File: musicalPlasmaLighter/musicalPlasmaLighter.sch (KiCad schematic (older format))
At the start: 13 parts, among them U1 ATtiny85-20SU, U2 LTC4054ES5-4.2, U3 74HCT00

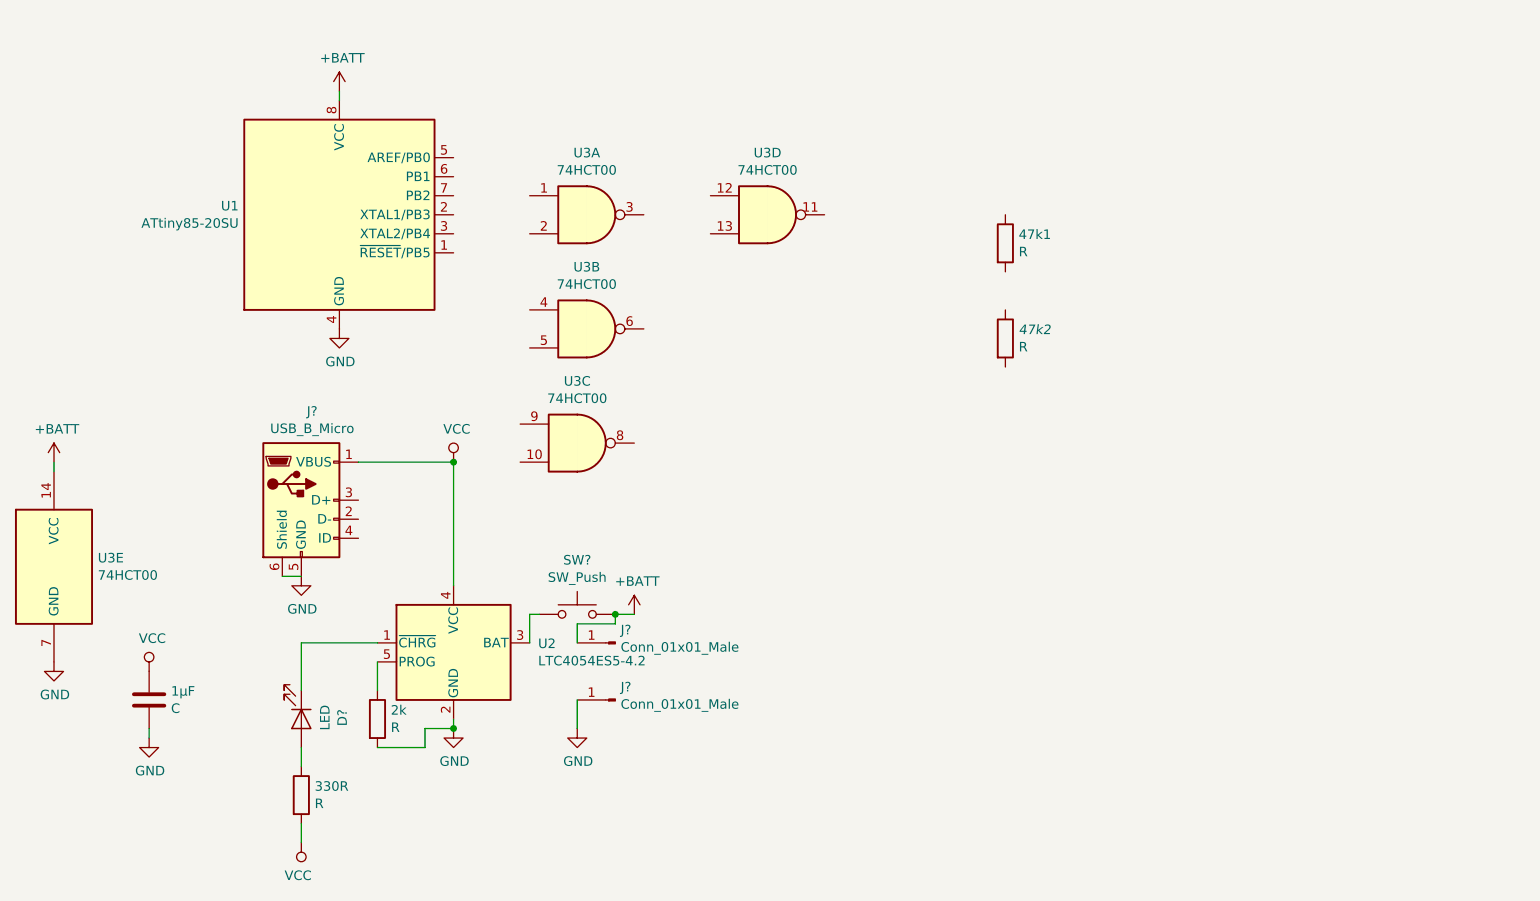
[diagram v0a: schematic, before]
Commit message: updated schematics
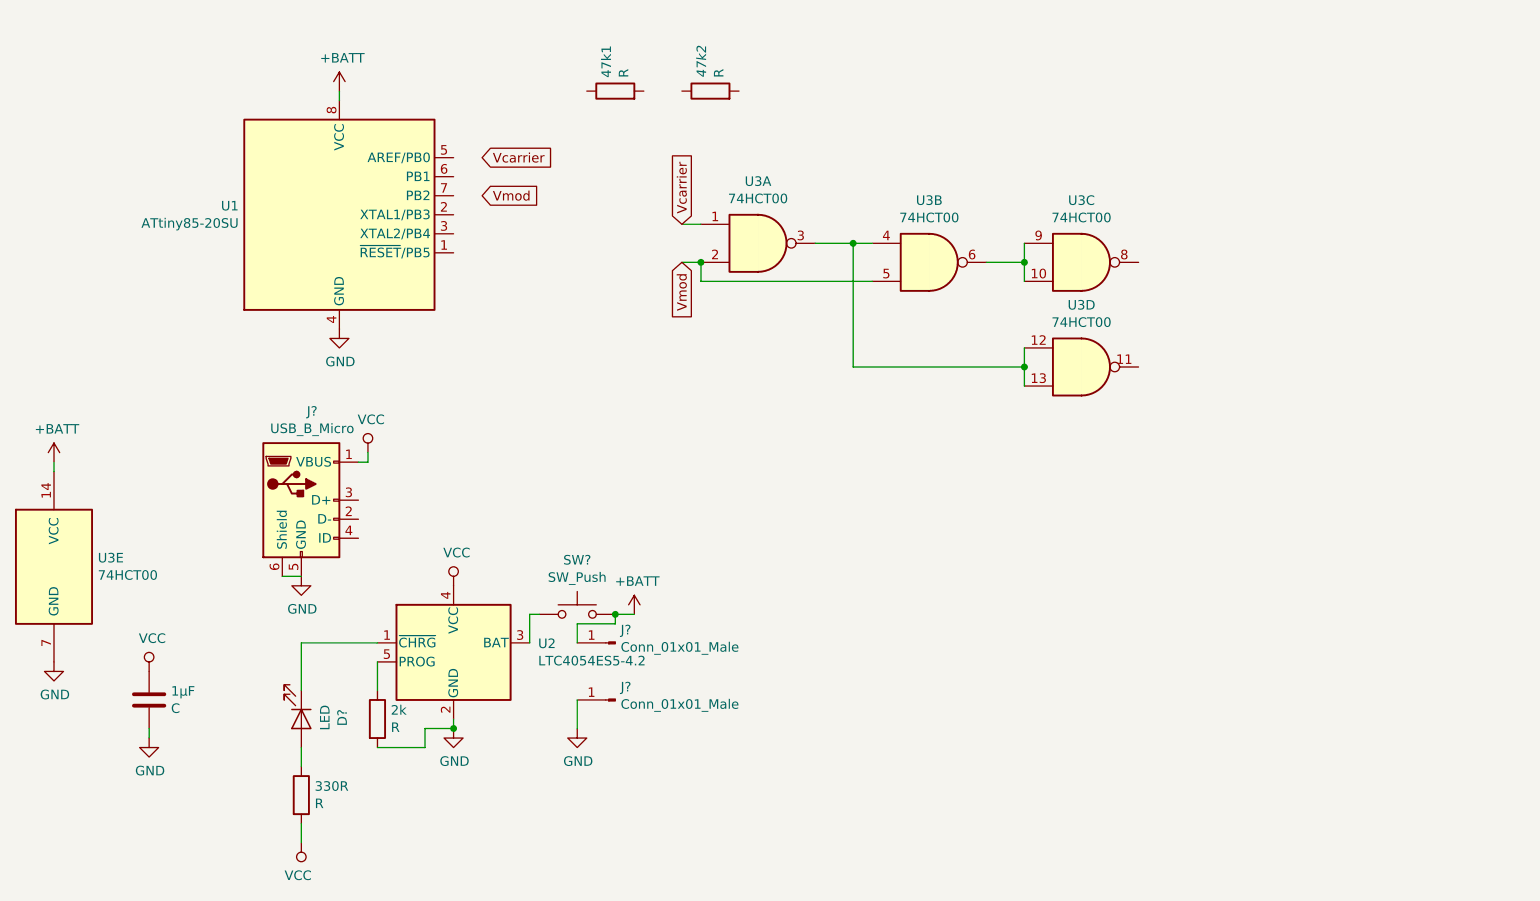
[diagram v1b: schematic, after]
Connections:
- net Vcarrier: now reaches U3.1
- net Vmod: now reaches U3.2
- net Vmod: now also U3.5
- net at U3.3: now also U3.12, U3.13, U3.4
- net at U3.6: now also U3.10, U3.9
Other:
- moved on the sheet: 47k1, 47k2, U3A, U3B, U3C, U3D
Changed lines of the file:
@@
 L 74xx:74HCT00 U3
 U 1 1 5D7430DD
-P 4000 1750
-F 0 "U3" H 4000 2075 50  0000 C CNN
-F 1 "74HCT00" H 4000 1984 50  0000 C CNN
-F 2 "Package_SO:TSSOP-14_4.4x5mm_P0.65mm" H 4000 1750 50  0001 C CNN
-F 3 "http://www.ti.com/lit/gpn/sn74hct00" H 4000 1750 50  0001 C CNN
-	1    4000 1750
+P 4900 1900
+F 0 "U3" H 4900 2225 50  0000 C CNN
+F 1 "74HCT00" H 4900 2134 50  0000 C CNN
+F 2 "Package_SO:TSSOP-14_4.4x5mm_P0.65mm" H 4900 1900 50  0001 C CNN
+F 3 "http://www.ti.com/lit/gpn/sn74hct00" H 4900 1900 50  0001 C CNN
+	1    4900 1900
 	1    0    0    -1
 $EndComp
@@
 L 74xx:74HCT00 U3
 U 2 1 5D744372
-P 4000 2350
-F 0 "U3" H 4000 2675 50  0000 C CNN
-F 1 "74HCT00" H 4000 2584 50  0000 C CNN
-F 2 "Package_SO:TSSOP-14_4.4x5mm_P0.65mm" H 4000 2350 50  0001 C CNN
-F 3 "http://www.ti.com/lit/gpn/sn74hct00" H 4000 2350 50  0001 C CNN
-	2    4000 2350
+P 5800 2000
+F 0 "U3" H 5800 2325 50  0000 C CNN
+F 1 "74HCT00" H 5800 2234 50  0000 C CNN
+F 2 "Package_SO:TSSOP-14_4.4x5mm_P0.65mm" H 5800 2000 50  0001 C CNN
+F 3 "http://www.ti.com/lit/gpn/sn74hct00" H 5800 2000 50  0001 C CNN
+	2    5800 2000
 	1    0    0    -1
 $EndComp
@@
 L 74xx:74HCT00 U3
 U 3 1 5D745C50
-P 3950 2950
-F 0 "U3" H 3950 3275 50  0000 C CNN
-F 1 "74HCT00" H 3950 3184 50  0000 C CNN
-F 2 "Package_SO:TSSOP-14_4.4x5mm_P0.65mm" H 3950 2950 50  0001 C CNN
-F 3 "http://www.ti.com/lit/gpn/sn74hct00" H 3950 2950 50  0001 C CNN
-	3    3950 2950
+P 6600 2000
+F 0 "U3" H 6600 2325 50  0000 C CNN
+F 1 "74HCT00" H 6600 2234 50  0000 C CNN
+F 2 "Package_SO:TSSOP-14_4.4x5mm_P0.65mm" H 6600 2000 50  0001 C CNN
+F 3 "http://www.ti.com/lit/gpn/sn74hct00" H 6600 2000 50  0001 C CNN
+	3    6600 2000
 	1    0    0    -1
 $EndComp
@@
 L 74xx:74HCT00 U3
 U 4 1 5D74715B
-P 4950 1750
-F 0 "U3" H 4950 2075 50  0000 C CNN
-F 1 "74HCT00" H 4950 1984 50  0000 C CNN
-F 2 "Package_SO:TSSOP-14_4.4x5mm_P0.65mm" H 4950 1750 50  0001 C CNN
-F 3 "http://www.ti.com/lit/gpn/sn74hct00" H 4950 1750 50  0001 C CNN
-	4    4950 1750
+P 6600 2550
+F 0 "U3" H 6600 2875 50  0000 C CNN
+F 1 "74HCT00" H 6600 2784 50  0000 C CNN
+F 2 "Package_SO:TSSOP-14_4.4x5mm_P0.65mm" H 6600 2550 50  0001 C CNN
+F 3 "http://www.ti.com/lit/gpn/sn74hct00" H 6600 2550 50  0001 C CNN
+	4    6600 2550
 	1    0    0    -1
 $EndComp
@@
 L Device:R 47k1
 U 1 1 5D750EC0
-P 6200 1900
-F 0 "47k1" H 6270 1946 50  0000 L CNN
-F 1 "R" H 6270 1855 50  0000 L CNN
-F 2 "Resistor_SMD:R_0603_1608Metric" V 6130 1900 50  0001 C CNN
-F 3 "~" H 6200 1900 50  0001 C CNN
-	1    6200 1900
-	1    0    0    -1
+P 4150 1100
+F 0 "47k1" H 4220 1146 50  0000 L CNN
+F 1 "R" H 4220 1055 50  0000 L CNN
+F 2 "Resistor_SMD:R_0603_1608Metric" V 4080 1100 50  0001 C CNN
+F 3 "~" H 4150 1100 50  0001 C CNN
+	1    4150 1100
+	0    -1   -1   0
 $EndComp
 $Comp
 L Device:R 47k2
 U 1 1 5D754E95
-P 6200 2400
-F 0 "47k2" H 6270 2446 50  0000 L CIN
-F 1 "R" H 6270 2355 50  0000 L CNN
-F 2 "Resistor_SMD:R_0603_1608Metric" V 6130 2400 50  0001 C CNN
-F 3 "~" H 6200 2400 50  0001 C CNN
-	1    6200 2400
-	1    0    0    -1
+P 4650 1100
+F 0 "47k2" H 4720 1146 50  0000 L CIN
+F 1 "R" H 4720 1055 50  0000 L CNN
+F 2 "Resistor_SMD:R_0603_1608Metric" V 4580 1100 50  0001 C CNN
+F 3 "~" H 4650 1100 50  0001 C CNN
+	1    4650 1100
+	0    -1   -1   0
 $EndComp
 $Comp
@@
 Wire Wire Line
 	2400 3650 2500 3650
-Wire Wire Line
-	2800 3050 3300 3050
 $Comp
 L power:VCC #PWR?
 U 1 1 5D840F00
-P 3300 3050
-F 0 "#PWR?" H 3300 2900 50  0001 C CNN
-F 1 "VCC" H 3317 3223 50  0000 C CNN
-F 2 "" H 3300 3050 50  0001 C CNN
-F 3 "" H 3300 3050 50  0001 C CNN
-	1    3300 3050
-	1    0    0    -1
-$EndComp
-Connection ~ 3300 3050
+P 2850 3000
+F 0 "#PWR?" H 2850 2850 50  0001 C CNN
+F 1 "VCC" H 2867 3173 50  0000 C CNN
+F 2 "" H 2850 3000 50  0001 C CNN
+F 3 "" H 2850 3000 50  0001 C CNN
+	1    2850 3000
+	1    0    0    -1
+$EndComp
 $Comp
 L Device:C 1µF
@@
 Wire Wire Line
 	2500 4000 2900 4000
-Wire Wire Line
-	3300 3050 3300 3700
 $Comp
 L Battery_Management:LTC4054ES5-4.2 U2
@@
 	3150 4450 3300 4450
 Connection ~ 3300 4450
+Wire Wire Line
+	2800 3050 2850 3050
+Wire Wire Line
+	2850 3050 2850 3000
+$Comp
+L power:VCC #PWR?
+U 1 1 5D884EBA
+P 3300 3700
+F 0 "#PWR?" H 3300 3550 50  0001 C CNN
+F 1 "VCC" H 3317 3873 50  0000 C CNN
+F 2 "" H 3300 3700 50  0001 C CNN
+F 3 "" H 3300 3700 50  0001 C CNN
+	1    3300 3700
+	1    0    0    -1
+$EndComp
+Wire Wire Line
+	4600 2000 4600 2100
+Wire Wire Line
+	4600 2100 5500 2100
+Wire Wire Line
+	6100 2000 6300 2000
+Wire Wire Line
+	6300 1900 6300 2000
+Connection ~ 6300 2000
+Wire Wire Line
+	6300 2000 6300 2100
+Wire Wire Line
+	6300 2550 6300 2650
+Wire Wire Line
+	6300 2450 6300 2550
+Connection ~ 6300 2550
+Wire Wire Line
+	5200 1900 5400 1900
+Wire Wire Line
+	5400 2550 5400 1900
+Wire Wire Line
+	5400 2550 6300 2550
+Connection ~ 5400 1900
+Wire Wire Line
+	5400 1900 5500 1900
+Text GLabel 4500 1800 1    50   Input ~ 0
+Vcarrier
+Text GLabel 4500 2000 3    50   Input ~ 0
+Vmod
+Wire Wire Line
+	4600 2000 4500 2000
+Connection ~ 4600 2000
+Wire Wire Line
+	4600 1800 4500 1800
+Text GLabel 3450 1450 2    50   Input ~ 0
+Vcarrier
+Text GLabel 3450 1650 2    50   Input ~ 0
+Vmod
 $EndSCHEMATC

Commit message: updated schematics
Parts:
- removed 1µF: C, symbol Device:C
- removed 2k, 330R: R, symbol Device:R
- removed D?: LED, symbol Device:LED
- removed J?: USB_B_Micro, symbol Connector:USB_B_Micro
- removed U2: LTC4054ES5-4.2, Package_TO_SOT_SMD:TSOT-23-5, symbol Battery_Management:LTC4054ES5-4.2
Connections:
- net labels removed: +BATT, VCC, Vcarrier, Vmod
- wire segments 35 -> 0

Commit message: updated schemaitcs
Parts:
- added 1µF1: C, symbol Device:C
- added 2k1, 330R1: R, symbol Device:R
- added D1: LED, symbol Device:LED
- added J1: USB_B_Micro, symbol Connector:USB_B_Micro
- added J2, J3, J4, J5: Conn_01x01_Male, symbol Connector:Conn_01x01_Male
- added Q? (x2): 85N3LH5, Package_TO_SOT_THT:TO-220-3_Vertical, symbol Transistor_FET:IRLZ44N
- added U2: LTC4054ES5-4.2, Package_TO_SOT_SMD:TSOT-23-5, symbol Battery_Management:LTC4054ES5-4.2
- gave numbers to parts that had none: 3
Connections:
- net labels added: +BATT, FET_A, FET_B, VCC, Vcarrier, Vmod
- wire segments 0 -> 55

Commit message: updated schemaitcs
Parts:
- added J8, J9: Conn_01x01_Male, TestPoint:TestPoint_Pad_2.0x2.0mm, symbol Connector:Conn_01x01_Male
- 1µF1: footprint (none) -> Capacitor_SMD:C_0603_1608Metric
- 2k1, 330R1: footprint (none) -> Resistor_SMD:R_0612_1632Metric
- D1: footprint (none) -> LED_SMD:LED_0603_1608Metric
- J1: footprint (none) -> Connector_USB:USB_Micro-B_GCT_USB3076-30-A
- J2, J3, J4, J5, J6, J7: footprint (none) -> TestPoint:TestPoint_Pad_2.0x2.0mm
- SW1: footprint (none) -> Button_Switch_SMD:Panasonic_EVQPUK_EVQPUB
- gave numbers to parts that had none: 2
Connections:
- net GND: now also 47k1.1, 47k2.1, Q1.3 (S), Q2.3 (S)
- net at Q1.2 (D): now also J8.1 (Pin_1)
- net at Q2.2 (D): now also J9.1 (Pin_1)
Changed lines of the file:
@@
 F 0 "SW1" H 3950 4135 50  0000 C CNN
 F 1 "SW_Push" H 3950 4044 50  0000 C CNN
-F 2 "" H 3950 4050 50  0001 C CNN
+F 2 "Button_Switch_SMD:Panasonic_EVQPUK_EVQPUB" H 3950 4050 50  0001 C CNN
 F 3 "~" H 3950 4050 50  0001 C CNN
 	1    3950 3850
@@
 F 0 "J6" H 4122 3932 50  0000 R CNN
 F 1 "Conn_01x01_Male" H 4122 4023 50  0000 R CNN
-F 2 "" H 4150 4000 50  0001 C CNN
+F 2 "TestPoint:TestPoint_Pad_2.0x2.0mm" H 4150 4000 50  0001 C CNN
 F 3 "~" H 4150 4000 50  0001 C CNN
 	1    4150 4000
@@
 F 0 "J7" H 4122 4232 50  0000 R CNN
 F 1 "Conn_01x01_Male" H 4122 4323 50  0000 R CNN
-F 2 "" H 4150 4300 50  0001 C CNN
+F 2 "TestPoint:TestPoint_Pad_2.0x2.0mm" H 4150 4300 50  0001 C CNN
 F 3 "~" H 4150 4300 50  0001 C CNN
 	1    4150 4300
@@
 F 0 "J1" H 2557 3717 50  0000 C CNN
 F 1 "USB_B_Micro" H 2557 3626 50  0000 C CNN
-F 2 "" H 2650 3200 50  0001 C CNN
+F 2 "Connector_USB:USB_Micro-B_GCT_USB3076-30-A" H 2650 3200 50  0001 C CNN
 F 3 "~" H 2650 3200 50  0001 C CNN
 	1    2500 3250
@@
 F 0 "1µF1" H 1815 4346 50  0000 L CNN
 F 1 "C" H 1815 4255 50  0000 L CNN
-F 2 "" H 1738 4150 50  0001 C CNN
+F 2 "Capacitor_SMD:C_0603_1608Metric" H 1738 4150 50  0001 C CNN
 F 3 "~" H 1700 4300 50  0001 C CNN
 	1    1700 4300
@@
 F 0 "D1" H 2493 4616 50  0000 C CNN
 F 1 "LED" H 2493 4525 50  0000 C CNN
-F 2 "" H 2500 4400 50  0001 C CNN
+F 2 "LED_SMD:LED_0603_1608Metric" H 2500 4400 50  0001 C CNN
 F 3 "~" H 2500 4400 50  0001 C CNN
 	1    2500 4400
@@
 F 0 "330R1" H 2570 4846 50  0000 L CNN
 F 1 "R" H 2570 4755 50  0000 L CNN
-F 2 "" V 2430 4800 50  0001 C CNN
+F 2 "Resistor_SMD:R_0612_1632Metric" V 2430 4800 50  0001 C CNN
 F 3 "~" H 2500 4800 50  0001 C CNN
 	1    2500 4800
@@
 F 0 "2k1" H 2970 4446 50  0000 L CNN
 F 1 "R" H 2970 4355 50  0000 L CNN
-F 2 "" V 2830 4400 50  0001 C CNN
+F 2 "Resistor_SMD:R_0612_1632Metric" V 2830 4400 50  0001 C CNN
 F 3 "~" H 2900 4400 50  0001 C CNN
 	1    2900 4400
@@
 F 0 "J2" H 3522 1882 50  0000 R CNN
 F 1 "Conn_01x01_Male" H 3522 1973 50  0000 R CNN
-F 2 "" H 3550 1950 50  0001 C CNN
+F 2 "TestPoint:TestPoint_Pad_2.0x2.0mm" H 3550 1950 50  0001 C CNN
 F 3 "~" H 3550 1950 50  0001 C CNN
 	1    3550 1950
@@
 F 0 "J3" H 3572 1382 50  0000 R CNN
 F 1 "Conn_01x01_Male" H 3572 1473 50  0000 R CNN
-F 2 "" H 3600 1450 50  0001 C CNN
+F 2 "TestPoint:TestPoint_Pad_2.0x2.0mm" H 3600 1450 50  0001 C CNN
 F 3 "~" H 3600 1450 50  0001 C CNN
 	1    3600 1450
@@
 F 0 "J4" H 3572 1482 50  0000 R CNN
 F 1 "Conn_01x01_Male" H 3572 1573 50  0000 R CNN
-F 2 "" H 3600 1550 50  0001 C CNN
+F 2 "TestPoint:TestPoint_Pad_2.0x2.0mm" H 3600 1550 50  0001 C CNN
 F 3 "~" H 3600 1550 50  0001 C CNN
 	1    3600 1550
@@
 F 0 "J5" H 3572 1582 50  0000 R CNN
 F 1 "Conn_01x01_Male" H 3572 1673 50  0000 R CNN
-F 2 "" H 3600 1650 50  0001 C CNN
+F 2 "TestPoint:TestPoint_Pad_2.0x2.0mm" H 3600 1650 50  0001 C CNN
 F 3 "~" H 3600 1650 50  0001 C CNN
 	1    3600 1650
@@
 FET_B
 $Comp
-L Transistor_FET:IRLZ44N Q?
+L Transistor_FET:IRLZ44N Q1
 U 1 1 5D7AF285
 P 8350 2050
-F 0 "Q?" H 8556 2096 50  0000 L CNN
+F 0 "Q1" H 8556 2096 50  0000 L CNN
 F 1 "85N3LH5" H 8556 2005 50  0000 L CNN
 F 2 "Package_TO_SOT_THT:TO-220-3_Vertical" H 8600 1975 50  0001 L CIN
@@
 $EndComp
 $Comp
-L Transistor_FET:IRLZ44N Q?
+L Transistor_FET:IRLZ44N Q2
 U 1 1 5D7B0D59
 P 8350 3000
-F 0 "Q?" H 8556 3046 50  0000 L CNN
+F 0 "Q2" H 8556 3046 50  0000 L CNN
 F 1 "85N3LH5" H 8556 2955 50  0000 L CNN
 F 2 "Package_TO_SOT_THT:TO-220-3_Vertical" H 8600 2925 50  0001 L CIN
@@
 Wire Wire Line
 	8450 2350 8450 2250
+$Comp
+L power:GND #PWR0114
+U 1 1 5D7EB221
+P 8450 2350
+F 0 "#PWR0114" H 8450 2100 50  0001 C CNN
+F 1 "GND" H 8455 2177 50  0000 C CNN
+F 2 "" H 8450 2350 50  0001 C CNN
+F 3 "" H 8450 2350 50  0001 C CNN
+	1    8450 2350
+	1    0    0    -1
+$EndComp
+Connection ~ 8450 2350
+$Comp
+L power:GND #PWR0115
+U 1 1 5D7EB8E9
+P 8450 3300
+F 0 "#PWR0115" H 8450 3050 50  0001 C CNN
+F 1 "GND" H 8455 3127 50  0000 C CNN
+F 2 "" H 8450 3300 50  0001 C CNN
+F 3 "" H 8450 3300 50  0001 C CNN
+	1    8450 3300
+	1    0    0    -1
+$EndComp
+Connection ~ 8450 3300
+$Comp
+L Connector:Conn_01x01_Male J8
+U 1 1 5D7F022C
+P 8450 1650
+F 0 "J8" H 8422 1582 50  0000 R CNN
+F 1 "Conn_01x01_Male" H 8422 1673 50  0000 R CNN
+F 2 "TestPoint:TestPoint_Pad_2.0x2.0mm" H 8450 1650 50  0001 C CNN
+F 3 "~" H 8450 1650 50  0001 C CNN
+	1    8450 1650
+	0    1    1    0
+$EndComp
+$Comp
+L Connector:Conn_01x01_Male J9
+U 1 1 5D7F153B
+P 8450 2600
+F 0 "J9" H 8422 2532 50  0000 R CNN
+F 1 "Conn_01x01_Male" H 8422 2623 50  0000 R CNN
+F 2 "TestPoint:TestPoint_Pad_2.0x2.0mm" H 8450 2600 50  0001 C CNN
+F 3 "~" H 8450 2600 50  0001 C CNN
+	1    8450 2600
+	0    1    1    0
+$EndComp
 $EndSCHEMATC

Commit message: updated pcb layout
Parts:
- 2k1, 330R1: footprint Resistor_SMD:R_0612_1632Metric -> Resistor_SMD:R_0603_1608Metric
- Q1, Q2: footprint Package_TO_SOT_THT:TO-220-3_Vertical -> Package_TO_SOT_SMD:TO-263-2
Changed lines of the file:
@@
 F 0 "330R1" H 2570 4846 50  0000 L CNN
 F 1 "R" H 2570 4755 50  0000 L CNN
-F 2 "Resistor_SMD:R_0612_1632Metric" V 2430 4800 50  0001 C CNN
+F 2 "Resistor_SMD:R_0603_1608Metric" V 2430 4800 50  0001 C CNN
 F 3 "~" H 2500 4800 50  0001 C CNN
 	1    2500 4800
@@
 F 0 "2k1" H 2970 4446 50  0000 L CNN
 F 1 "R" H 2970 4355 50  0000 L CNN
-F 2 "Resistor_SMD:R_0612_1632Metric" V 2830 4400 50  0001 C CNN
+F 2 "Resistor_SMD:R_0603_1608Metric" V 2830 4400 50  0001 C CNN
 F 3 "~" H 2900 4400 50  0001 C CNN
 	1    2900 4400
@@
 F 0 "Q1" H 8556 2096 50  0000 L CNN
 F 1 "85N3LH5" H 8556 2005 50  0000 L CNN
-F 2 "Package_TO_SOT_THT:TO-220-3_Vertical" H 8600 1975 50  0001 L CIN
+F 2 "Package_TO_SOT_SMD:TO-263-2" H 8600 1975 50  0001 L CIN
 F 3 "http://www.irf.com/product-info/datasheets/data/irlz44n.pdf" H 8350 2050 50  0001 L CNN
 	1    8350 2050
@@
 F 0 "Q2" H 8556 3046 50  0000 L CNN
 F 1 "85N3LH5" H 8556 2955 50  0000 L CNN
-F 2 "Package_TO_SOT_THT:TO-220-3_Vertical" H 8600 2925 50  0001 L CIN
+F 2 "Package_TO_SOT_SMD:TO-263-2" H 8600 2925 50  0001 L CIN
 F 3 "http://www.irf.com/product-info/datasheets/data/irlz44n.pdf" H 8350 3000 50  0001 L CNN
 	1    8350 3000

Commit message: edited pcb
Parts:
- J2, J3, J4, J5: footprint TestPoint:TestPoint_Pad_2.0x2.0mm -> TestPoint:TestPoint_Pad_1.5x1.5mm
- Q1, Q2: footprint Package_TO_SOT_SMD:TO-263-2 -> Package_TO_SOT_SMD:TO-252-2
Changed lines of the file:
@@
 F 0 "J2" H 3522 1882 50  0000 R CNN
 F 1 "Conn_01x01_Male" H 3522 1973 50  0000 R CNN
-F 2 "TestPoint:TestPoint_Pad_2.0x2.0mm" H 3550 1950 50  0001 C CNN
+F 2 "TestPoint:TestPoint_Pad_1.5x1.5mm" H 3550 1950 50  0001 C CNN
 F 3 "~" H 3550 1950 50  0001 C CNN
 	1    3550 1950
@@
 F 0 "J3" H 3572 1382 50  0000 R CNN
 F 1 "Conn_01x01_Male" H 3572 1473 50  0000 R CNN
-F 2 "TestPoint:TestPoint_Pad_2.0x2.0mm" H 3600 1450 50  0001 C CNN
+F 2 "TestPoint:TestPoint_Pad_1.5x1.5mm" H 3600 1450 50  0001 C CNN
 F 3 "~" H 3600 1450 50  0001 C CNN
 	1    3600 1450
@@
 F 0 "J4" H 3572 1482 50  0000 R CNN
 F 1 "Conn_01x01_Male" H 3572 1573 50  0000 R CNN
-F 2 "TestPoint:TestPoint_Pad_2.0x2.0mm" H 3600 1550 50  0001 C CNN
+F 2 "TestPoint:TestPoint_Pad_1.5x1.5mm" H 3600 1550 50  0001 C CNN
 F 3 "~" H 3600 1550 50  0001 C CNN
 	1    3600 1550
@@
 F 0 "J5" H 3572 1582 50  0000 R CNN
 F 1 "Conn_01x01_Male" H 3572 1673 50  0000 R CNN
-F 2 "TestPoint:TestPoint_Pad_2.0x2.0mm" H 3600 1650 50  0001 C CNN
+F 2 "TestPoint:TestPoint_Pad_1.5x1.5mm" H 3600 1650 50  0001 C CNN
 F 3 "~" H 3600 1650 50  0001 C CNN
 	1    3600 1650
@@
 F 0 "Q1" H 8556 2096 50  0000 L CNN
 F 1 "85N3LH5" H 8556 2005 50  0000 L CNN
-F 2 "Package_TO_SOT_SMD:TO-263-2" H 8600 1975 50  0001 L CIN
+F 2 "Package_TO_SOT_SMD:TO-252-2" H 8600 1975 50  0001 L CIN
 F 3 "http://www.irf.com/product-info/datasheets/data/irlz44n.pdf" H 8350 2050 50  0001 L CNN
 	1    8350 2050
@@
 F 0 "Q2" H 8556 3046 50  0000 L CNN
 F 1 "85N3LH5" H 8556 2955 50  0000 L CNN
-F 2 "Package_TO_SOT_SMD:TO-263-2" H 8600 2925 50  0001 L CIN
+F 2 "Package_TO_SOT_SMD:TO-252-2" H 8600 2925 50  0001 L CIN
 F 3 "http://www.irf.com/product-info/datasheets/data/irlz44n.pdf" H 8350 3000 50  0001 L CNN
 	1    8350 3000
